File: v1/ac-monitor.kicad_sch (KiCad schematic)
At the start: 3 parts, among them U5 MID400S

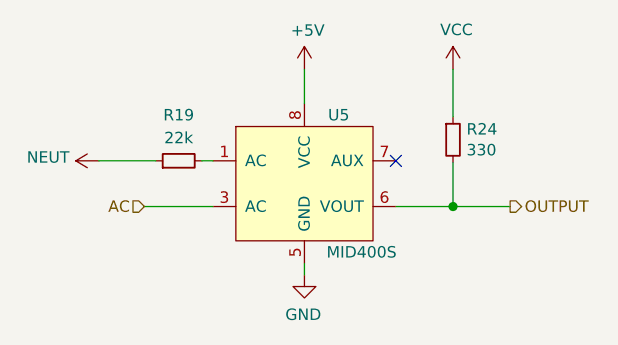
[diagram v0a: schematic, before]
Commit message: Add another blocker C
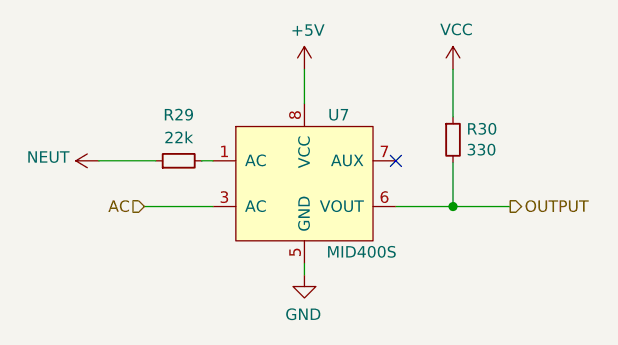
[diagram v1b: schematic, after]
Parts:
- renumbered R19 to R29, R24 to R30, U5 to U7
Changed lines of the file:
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@@
   (symbol (lib_id "power:NEUT") (at 80.645 66.04 90)
     (in_bom yes) (on_board yes)
-    (property "Reference" "#PWR025" (id 0) (at 84.455 66.04 0)
+    (property "Reference" "#PWR041" (id 0) (at 84.455 66.04 0)
       (effects (font (size 1.27 1.27)) hide)
     )
@@
   (symbol (lib_id "power:+5V") (at 103.505 55.88 0)
     (in_bom yes) (on_board yes)
-    (property "Reference" "#PWR0101" (id 0) (at 103.505 59.69 0)
+    (property "Reference" "#PWR042" (id 0) (at 103.505 59.69 0)
       (effects (font (size 1.27 1.27)) hide)
     )
@@
   (symbol (lib_id "power:VCC") (at 120.015 55.88 0)
     (in_bom yes) (on_board yes)
-    (property "Reference" "#PWR028" (id 0) (at 120.015 59.69 0)
+    (property "Reference" "#PWR044" (id 0) (at 120.015 59.69 0)
       (effects (font (size 1.27 1.27)) hide)
     )
@@
   (symbol (lib_id "power:GND") (at 103.505 78.74 0) (mirror y)
     (in_bom yes) (on_board yes)
-    (property "Reference" "#PWR030" (id 0) (at 103.505 85.09 0)
+    (property "Reference" "#PWR043" (id 0) (at 103.505 85.09 0)
       (effects (font (size 1.27 1.27)) hide)
     )
@@
   (symbol (lib_id "Device:R_Small") (at 89.535 66.04 90)
     (in_bom yes) (on_board yes)
-    (property "Reference" "R19" (id 0) (at 89.535 60.96 90))
+    (property "Reference" "R29" (id 0) (at 89.535 60.96 90))
     (property "Value" "22k" (id 1) (at 89.535 63.5 90))
     (property "Footprint" "Resistor_SMD:R_0603_1608Metric_Pad1.05x0.95mm_HandSolder" (id 2) (at 89.535 66.04 0)
@@
   (symbol (lib_id "Device:R_Small") (at 120.015 63.7032 0)
     (in_bom yes) (on_board yes)
-    (property "Reference" "R24" (id 0) (at 121.5136 62.5348 0)
+    (property "Reference" "R30" (id 0) (at 121.5136 62.5348 0)
       (effects (font (size 1.27 1.27)) (justify left))
     )
@@
   (symbol (lib_id "Isolator:MID400S") (at 103.505 68.58 0)
     (in_bom yes) (on_board yes)
-    (property "Reference" "U5" (id 0) (at 107.315 60.96 0))
+    (property "Reference" "U7" (id 0) (at 107.315 60.96 0))
     (property "Value" "MID400S" (id 1) (at 109.855 76.2 0))
     (property "Footprint" "Package_DIP:DIP-8_W7.62mm" (id 2) (at 103.505 68.58 0)

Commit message: more work
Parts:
- renumbered R29 to R27, R30 to R28, U7 to U6
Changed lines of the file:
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@@
   (symbol (lib_id "power:NEUT") (at 80.645 66.04 90)
     (in_bom yes) (on_board yes)
-    (property "Reference" "#PWR041" (id 0) (at 84.455 66.04 0)
+    (property "Reference" "#PWR037" (id 0) (at 84.455 66.04 0)
       (effects (font (size 1.27 1.27)) hide)
     )
@@
   (symbol (lib_id "power:+5V") (at 103.505 55.88 0)
     (in_bom yes) (on_board yes)
-    (property "Reference" "#PWR042" (id 0) (at 103.505 59.69 0)
+    (property "Reference" "#PWR038" (id 0) (at 103.505 59.69 0)
       (effects (font (size 1.27 1.27)) hide)
     )
@@
   (symbol (lib_id "power:VCC") (at 120.015 55.88 0)
     (in_bom yes) (on_board yes)
-    (property "Reference" "#PWR044" (id 0) (at 120.015 59.69 0)
+    (property "Reference" "#PWR040" (id 0) (at 120.015 59.69 0)
       (effects (font (size 1.27 1.27)) hide)
     )
@@
   (symbol (lib_id "power:GND") (at 103.505 78.74 0) (mirror y)
     (in_bom yes) (on_board yes)
-    (property "Reference" "#PWR043" (id 0) (at 103.505 85.09 0)
+    (property "Reference" "#PWR039" (id 0) (at 103.505 85.09 0)
       (effects (font (size 1.27 1.27)) hide)
     )
@@
   (symbol (lib_id "Device:R_Small") (at 89.535 66.04 90)
     (in_bom yes) (on_board yes)
-    (property "Reference" "R29" (id 0) (at 89.535 60.96 90))
+    (property "Reference" "R27" (id 0) (at 89.535 60.96 90))
     (property "Value" "22k" (id 1) (at 89.535 63.5 90))
     (property "Footprint" "Resistor_SMD:R_0603_1608Metric_Pad1.05x0.95mm_HandSolder" (id 2) (at 89.535 66.04 0)
@@
   (symbol (lib_id "Device:R_Small") (at 120.015 63.7032 0)
     (in_bom yes) (on_board yes)
-    (property "Reference" "R30" (id 0) (at 121.5136 62.5348 0)
+    (property "Reference" "R28" (id 0) (at 121.5136 62.5348 0)
       (effects (font (size 1.27 1.27)) (justify left))
     )
@@
   (symbol (lib_id "Isolator:MID400S") (at 103.505 68.58 0)
     (in_bom yes) (on_board yes)
-    (property "Reference" "U7" (id 0) (at 107.315 60.96 0))
+    (property "Reference" "U6" (id 0) (at 107.315 60.96 0))
     (property "Value" "MID400S" (id 1) (at 109.855 76.2 0))
     (property "Footprint" "Package_DIP:DIP-8_W7.62mm" (id 2) (at 103.505 68.58 0)

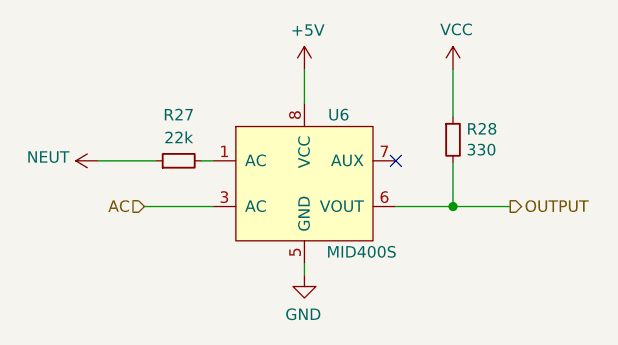
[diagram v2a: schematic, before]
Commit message: Update to new KiCad symbols, replace and turn D1 module
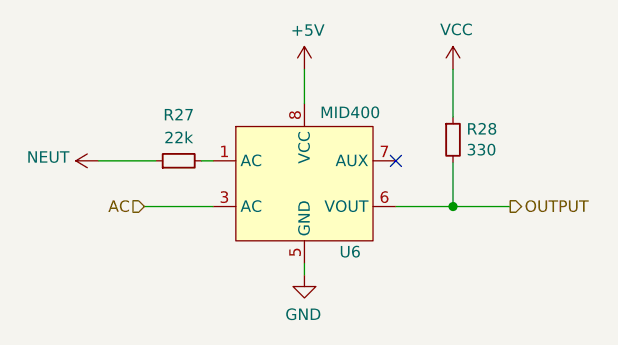
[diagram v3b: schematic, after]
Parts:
- removed U6: MID400S, Package_DIP:DIP-8_W7.62mm, symbol Isolator:MID400S
- added U6: MID400, Package_DIP:DIP-8_W7.62mm, symbol Isolator:MID400
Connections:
- net +5V: now also U6.8 (VCC)
- net AC: now also U6.3 (AC)
- net GND: now also U6.5 (GND)
- net OUTPUT: now also U6.6 (VOUT)
- net at R27.2: now also U6.1 (AC)
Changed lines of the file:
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@@
     )
   )
-  (symbol (lib_id "Isolator:MID400S") (at 103.505 68.58 0)
+  (symbol (lib_id "Isolator:MID400") (at 103.505 68.58 0)
     (in_bom yes) (on_board yes)
-    (property "Reference" "U6" (id 0) (at 107.315 60.96 0))
-    (property "Value" "MID400S" (id 1) (at 109.855 76.2 0))
+    (property "Reference" "U6" (id 0) (at 108.585 76.1808 0))
+    (property "Value" "MID400" (id 1) (at 108.585 60.6995 0))
     (property "Footprint" "Package_DIP:DIP-8_W7.62mm" (id 2) (at 103.505 68.58 0)
       (effects (font (size 1.27 1.27)) hide)
